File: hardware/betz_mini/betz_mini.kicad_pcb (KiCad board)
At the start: 4 copper layers, 40 x 40 mm, 62 parts, among them J1 upstream, J2 downstream, J3 ARM SWD, J4 BLDC, J5 BONUS, J6 EXTRA_BONUS, U1 stm32g474ceu6, U2 AS5047U, U3 IIS328DQ, U4 MP6540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

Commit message: update part numbers
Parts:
- C4, C5: value 22u -> 10u

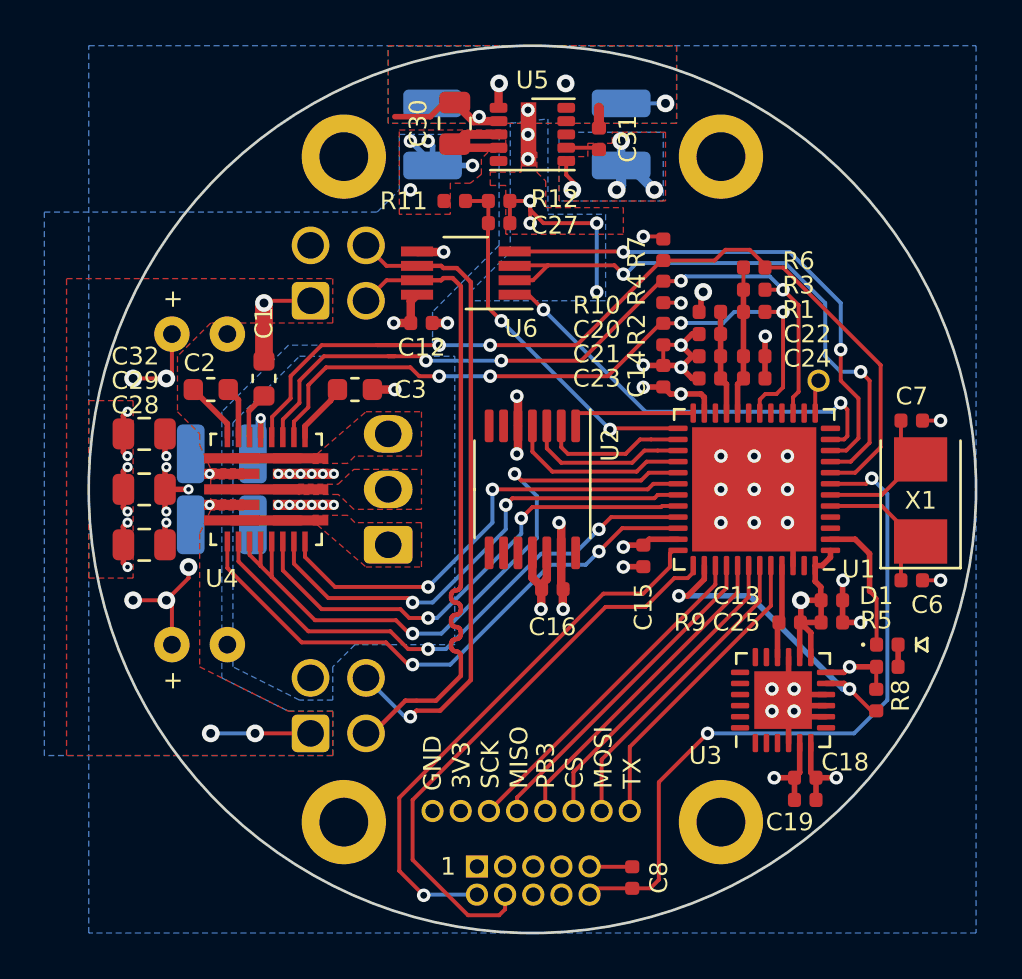
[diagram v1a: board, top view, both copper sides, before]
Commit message: route low-side pwm so that MP6540A can also work on this board
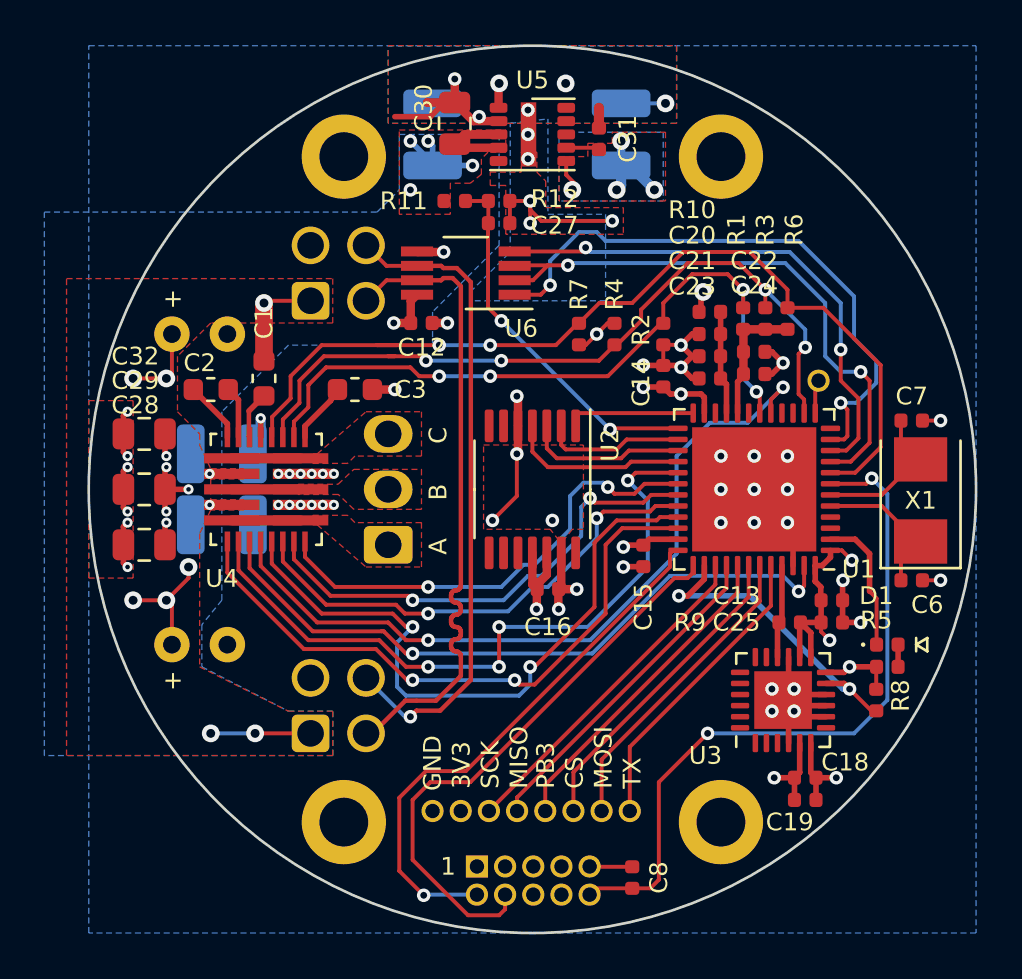
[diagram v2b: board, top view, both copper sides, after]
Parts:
- moved R7 5.37 mm to (152.1, 93.0), turned to -90 degrees
- moved R4 2.91 mm to (153.7, 93.0), turned to 90 degrees
- moved R6 2.75 mm to (161.5, 92.3), turned to 90 degrees
- moved R3 1.39 mm to (160.5, 92.3), turned to 90 degrees
- moved R1 0.58 mm to (159.5, 92.3), turned to 90 degrees
- moved C16 0.20 mm to (150.7, 104.5)
- moved C22 0.20 mm to (160.0, 93.8)
- moved C24 0.20 mm to (160.0, 94.8)
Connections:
- net /PWMA renamed /HSA
- net /PWMB renamed /HSB
- net /PWMC renamed /HSC
- U1 pad 14: Net-(U1-Pad14) -> /IB
- U1 pad 15: /IB -> Net-(U1-Pad15)
- U1 pad 17: Net-(U1-Pad17) -> /LSB
- U1 pad 29: /BLDC_EN -> /SLEEP
- U1 pad 33: /SLEEP -> /LSC
- U1 pad 47: Net-(U1-Pad47) -> /LSA
- U4 pad 3: /BLDC_EN -> /LSA
- U4 pad 4: /BLDC_EN -> /LSB
- U4 pad 5: /BLDC_EN -> /LSC
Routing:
- net /LSB: track 0.00 -> 34.7 mm, vias 0 -> 2
- net /LSA: track 0.00 -> 30.6 mm, vias 0 -> 2
- net /BLDC_EN: track 30.4 -> 0.00 mm, vias 2 -> 0
- net /LSC: track 0.00 -> 29.9 mm, vias 0 -> 2
- net /RS485_RO: track 19.5 -> 27.1 mm
- net /SLEEP: track 24.8 -> 31.2 mm, vias 2 -> 4
- net GND: track 88.7 -> 92.0 mm, vias 62 -> 63
- net /FAULT: track 25.9 -> 28.5 mm
- net /VREF: track 6.67 -> 5.56 mm
- net /IB: track 34.1 -> 34.7 mm
- net +3V3: track 37.9 -> 37.8 mm, vias 13 -> 14
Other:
- board text added: "C"

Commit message: hopefully last bit of PCB cleanup.
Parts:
- added TP1: TestPoint_Small, TestPoint:TestPoint_Pad_D1.0mm, F.Cu at (153.5, 95.1)
- added TP10: TestPoint_Small, TestPoint:TestPoint_Pad_D1.0mm, B.Cu at (158.6, 103.9)
- added TP11: TestPoint_Small, TestPoint:TestPoint_Pad_D1.0mm, B.Cu at (159.0, 97.0)
- added TP12: TestPoint_Small, TestPoint:TestPoint_Pad_D1.0mm, F.Cu at (150.5, 107.0)
- added TP13: TestPoint_Small, TestPoint:TestPoint_Pad_D1.0mm, B.Cu at (152.8, 102.8)
- added TP14: TestPoint_Small, TestPoint:TestPoint_Pad_D1.0mm, B.Cu at (151.8, 100.9)
- added TP15: TestPoint_Small, TestPoint:TestPoint_Pad_D1.0mm, B.Cu at (152.5, 99.1)
- added TP16: TestPoint_Small, TestPoint:TestPoint_Pad_D1.0mm, F.Cu at (153.7, 104.7)
- added TP2: TestPoint_Small, TestPoint:TestPoint_Pad_D1.0mm, F.Cu at (155.5, 90.5)
- added TP3: TestPoint_Small, TestPoint:TestPoint_Pad_D1.0mm, F.Cu at (153.2, 91.0)
- added TP4: TestPoint_Small, TestPoint:TestPoint_Pad_D1.0mm, B.Cu at (165.0, 96.1)
- added TP5: TestPoint_Small, TestPoint:TestPoint_Pad_D1.0mm, B.Cu at (163.0, 91.9)
- added TP6: TestPoint_Small, TestPoint:TestPoint_Pad_D1.0mm, B.Cu at (162.3, 89.9)
- added TP7: TestPoint_Small, TestPoint:TestPoint_Pad_D1.0mm, B.Cu at (163.0, 108.0)
- added TP8: TestPoint_Small, TestPoint:TestPoint_Pad_D1.0mm, B.Cu at (160.2, 105.2)
- added TP9: TestPoint_Small, TestPoint:TestPoint_Pad_D1.0mm, B.Cu at (154.6, 100.8)
- moved LOGO1 4.60 mm to (164.8, 100.0)
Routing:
- net /ACCEL_SDA: track 4.21 -> 5.94 mm, vias 0 -> 1
- net /HSC: track 21.3 -> 22.6 mm
- net /RS485_RO: track 27.1 -> 27.6 mm
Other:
- board text added: "-D+"
- board text added: "BETZ MINI REV A 5/2020"
- board text added: "D+"
- board text added: "D-"
- board text added: "DE"
- board text added: "DI"
- board text added: "FAULT"
- board text added: "HSA"
- board text added: "HSB"
- board text added: "HSC"
- board text added: "IA"
- board text added: "IB"
- board text added: "IC"
- board text added: "LSA"
- board text added: "LSB"
- board text added: "LSC"
- board text added: "RO"
- board text added: "SCL"
- board text added: "SDA"
- board text added: "SLP"
- board text removed: "BETZ MINI REV A MAY 2020"
